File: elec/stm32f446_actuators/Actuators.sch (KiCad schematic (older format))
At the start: 105 parts, among them IC1 TS2596CM550_RNG, J11 1, J13 2, J15 3, J17 0, J18 4, J19 4, J21 0, J22 3, J23 1, J24 5, J25 5, J27 1, J28 4, J29 +VBAT, J30 2, J31 6, J32 2, J33 5, J34 +5V, J35 GND, J36 3, J37 7, J38 Conn_01x04, J39 Conn_01x04, J40 0, J41 2, J42 4, J43 Conn_01x04, J44 Conn_01x04, J45 1, J46 3, J5 0, J6 Conn_01x04, J7 Conn_01x04, J8 1, J9 0, Q1 IRLZ44N, Q11 IRLZ44N, Q3 IRLZ44N, Q5 IRLZ44N, Q7 IRLZ44N, Q9 IRLZ44N

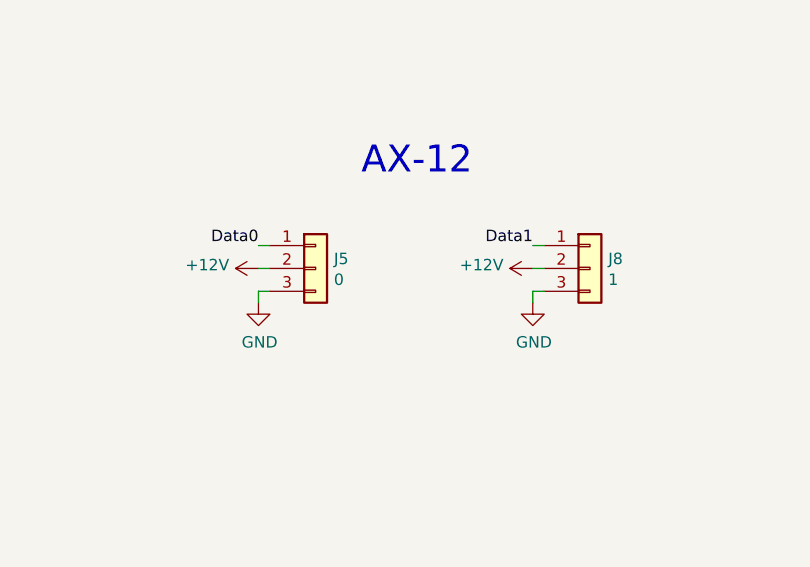
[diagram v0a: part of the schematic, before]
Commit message: Fix serial 3 and 5 reversed labels
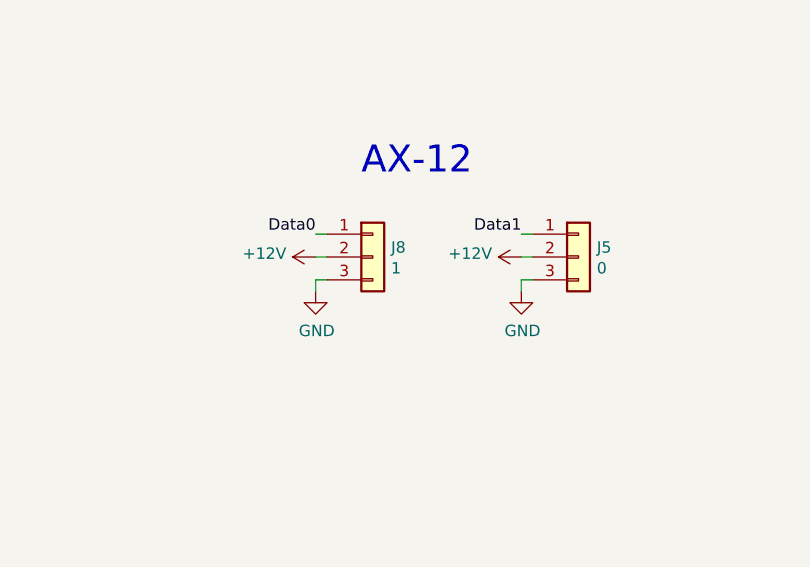
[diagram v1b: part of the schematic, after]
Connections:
- net RX3: now also J8.1 (Pin_1); no longer J5.1 (Pin_1)
- net RX5: now also J5.1 (Pin_1); no longer J8.1 (Pin_1)
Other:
- moved on the sheet: J5, J8
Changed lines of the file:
@@
 L Connector_Generic:Conn_01x03 J5
 U 1 1 5E997112
-P 3500 10300
-F 0 "J5" H 3580 10342 50  0000 L CNN
-F 1 "0" H 3580 10251 50  0000 L CNN
-F 2 "Connector_Molex:Molex_SPOX_5267-03A_1x03_P2.50mm_Vertical" H 3500 10300 50  0001 C CNN
-F 3 "~" H 3500 10300 50  0001 C CNN
-	1    3500 10300
+P 4650 10250
+F 0 "J5" H 4730 10292 50  0000 L CNN
+F 1 "0" H 4730 10201 50  0000 L CNN
+F 2 "Connector_Molex:Molex_SPOX_5267-03A_1x03_P2.50mm_Vertical" H 4650 10250 50  0001 C CNN
+F 3 "~" H 4650 10250 50  0001 C CNN
+	1    4650 10250
 	1    0    0    -1
 $EndComp
@@
 L power:GND #PWR047
 U 1 1 5E768720
-P 3250 10450
-F 0 "#PWR047" H 3250 10200 50  0001 C CNN
-F 1 "GND" H 3255 10277 50  0000 C CNN
-F 2 "" H 3250 10450 50  0001 C CNN
-F 3 "" H 3250 10450 50  0001 C CNN
-	1    3250 10450
+P 4400 10400
+F 0 "#PWR047" H 4400 10150 50  0001 C CNN
+F 1 "GND" H 4405 10227 50  0000 C CNN
+F 2 "" H 4400 10400 50  0001 C CNN
+F 3 "" H 4400 10400 50  0001 C CNN
+	1    4400 10400
 	1    0    0    -1
 $EndComp
@@
 L power:+12V #PWR046
 U 1 1 5E7698FC
-P 3250 10300
-F 0 "#PWR046" H 3250 10150 50  0001 C CNN
-F 1 "+12V" V 3265 10428 50  0000 L CNN
-F 2 "" H 3250 10300 50  0001 C CNN
-F 3 "" H 3250 10300 50  0001 C CNN
-	1    3250 10300
+P 4400 10250
+F 0 "#PWR046" H 4400 10100 50  0001 C CNN
+F 1 "+12V" V 4415 10378 50  0000 L CNN
+F 2 "" H 4400 10250 50  0001 C CNN
+F 3 "" H 4400 10250 50  0001 C CNN
+	1    4400 10250
 	0    -1   -1   0
 $EndComp
-Text Label 3250 10200 2    50   ~ 0
+Text Label 3500 10150 2    50   ~ 0
 Data0
 Wire Wire Line
-	3250 10200 3300 10200
-Wire Wire Line
-	3300 10300 3250 10300
-Wire Wire Line
-	3250 10450 3250 10400
-Wire Wire Line
-	3250 10400 3300 10400
+	4400 10150 4450 10150
+Wire Wire Line
+	4450 10250 4400 10250
+Wire Wire Line
+	4400 10400 4400 10350
+Wire Wire Line
+	4400 10350 4450 10350
 $Comp
 L power:GND #PWR051
 U 1 1 5E7855A1
-P 4450 10450
-F 0 "#PWR051" H 4450 10200 50  0001 C CNN
-F 1 "GND" H 4455 10277 50  0000 C CNN
-F 2 "" H 4450 10450 50  0001 C CNN
-F 3 "" H 4450 10450 50  0001 C CNN
-	1    4450 10450
+P 3500 10400
+F 0 "#PWR051" H 3500 10150 50  0001 C CNN
+F 1 "GND" H 3505 10227 50  0000 C CNN
+F 2 "" H 3500 10400 50  0001 C CNN
+F 3 "" H 3500 10400 50  0001 C CNN
+	1    3500 10400
 	1    0    0    -1
 $EndComp
@@
 L power:+12V #PWR050
 U 1 1 5E7855A7
-P 4450 10300
-F 0 "#PWR050" H 4450 10150 50  0001 C CNN
-F 1 "+12V" V 4465 10428 50  0000 L CNN
-F 2 "" H 4450 10300 50  0001 C CNN
-F 3 "" H 4450 10300 50  0001 C CNN
-	1    4450 10300
+P 3500 10250
+F 0 "#PWR050" H 3500 10100 50  0001 C CNN
+F 1 "+12V" V 3515 10378 50  0000 L CNN
+F 2 "" H 3500 10250 50  0001 C CNN
+F 3 "" H 3500 10250 50  0001 C CNN
+	1    3500 10250
 	0    -1   -1   0
 $EndComp
-Text Label 4450 10200 2    50   ~ 0
+Text Label 4400 10150 2    50   ~ 0
 Data1
 Wire Wire Line
-	4450 10200 4500 10200
-Wire Wire Line
-	4500 10300 4450 10300
-Wire Wire Line
-	4450 10450 4450 10400
-Wire Wire Line
-	4450 10400 4500 10400
+	3500 10150 3550 10150
+Wire Wire Line
+	3550 10250 3500 10250
+Wire Wire Line
+	3500 10400 3500 10350
+Wire Wire Line
+	3500 10350 3550 10350
 $Comp
 L power:GND #PWR0147
@@
 L Connector_Generic:Conn_01x03 J8
 U 1 1 5E78559B
-P 4700 10300
-F 0 "J8" H 4780 10342 50  0000 L CNN
-F 1 "1" H 4780 10251 50  0000 L CNN
-F 2 "Connector_Molex:Molex_SPOX_5267-03A_1x03_P2.50mm_Vertical" H 4700 10300 50  0001 C CNN
-F 3 "~" H 4700 10300 50  0001 C CNN
-	1    4700 10300
-	1    0    0    -1
-$EndComp
+P 3750 10250
+F 0 "J8" H 3830 10292 50  0000 L CNN
+F 1 "1" H 3830 10201 50  0000 L CNN
+F 2 "Connector_Molex:Molex_SPOX_5267-03A_1x03_P2.50mm_Vertical" H 3750 10250 50  0001 C CNN
+F 3 "~" H 3750 10250 50  0001 C CNN
+	1    3750 10250
+	1    0    0    -1
+$EndComp
